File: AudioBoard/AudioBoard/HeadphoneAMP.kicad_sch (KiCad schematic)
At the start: 0 parts

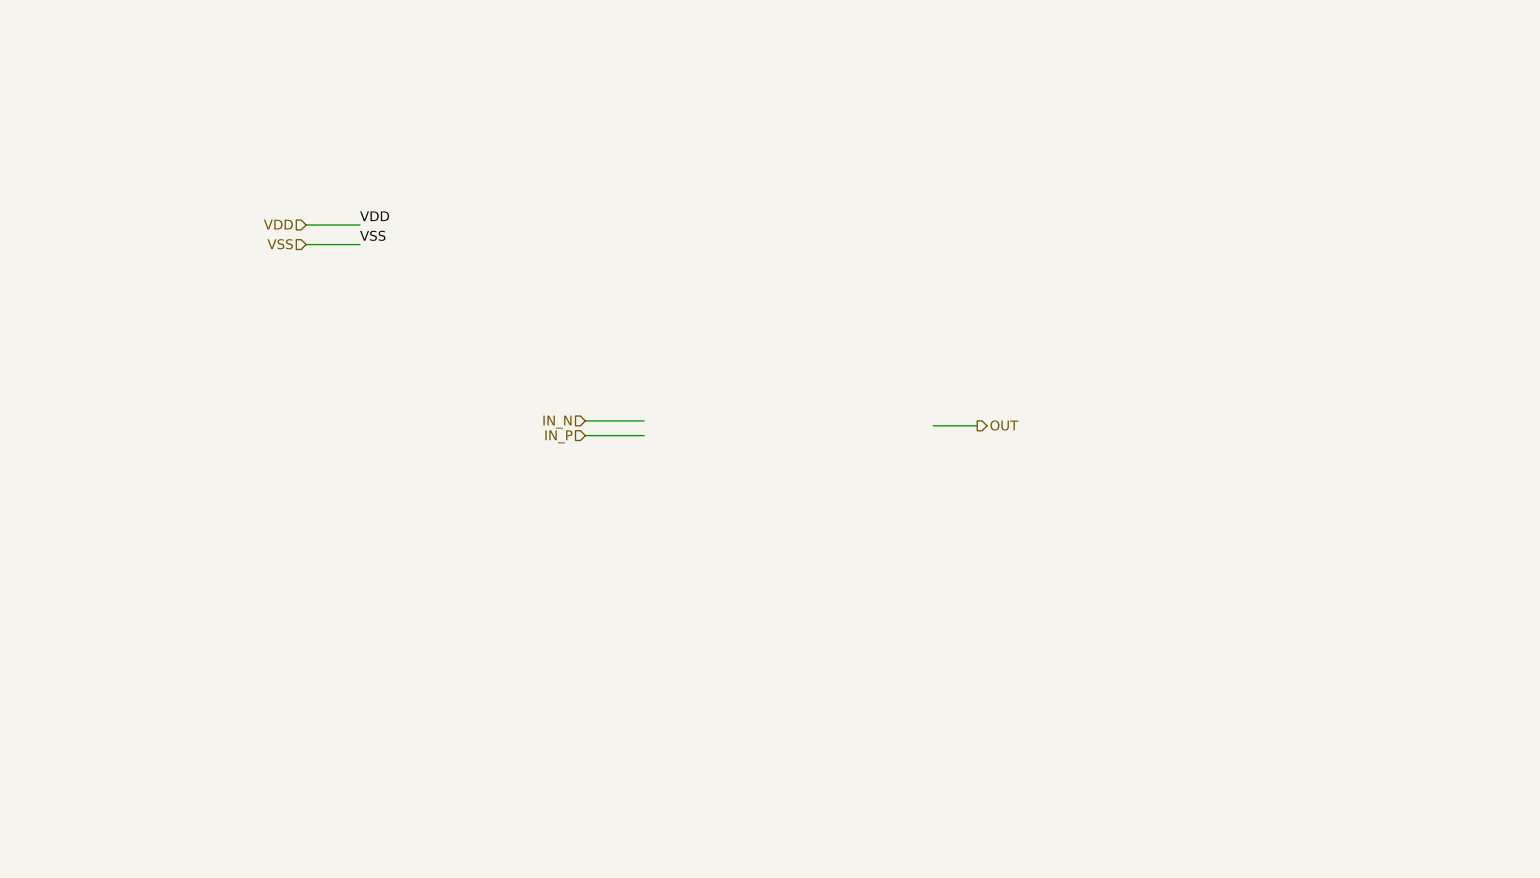
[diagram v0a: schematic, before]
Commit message: added jack IO, headphone amp cirucit
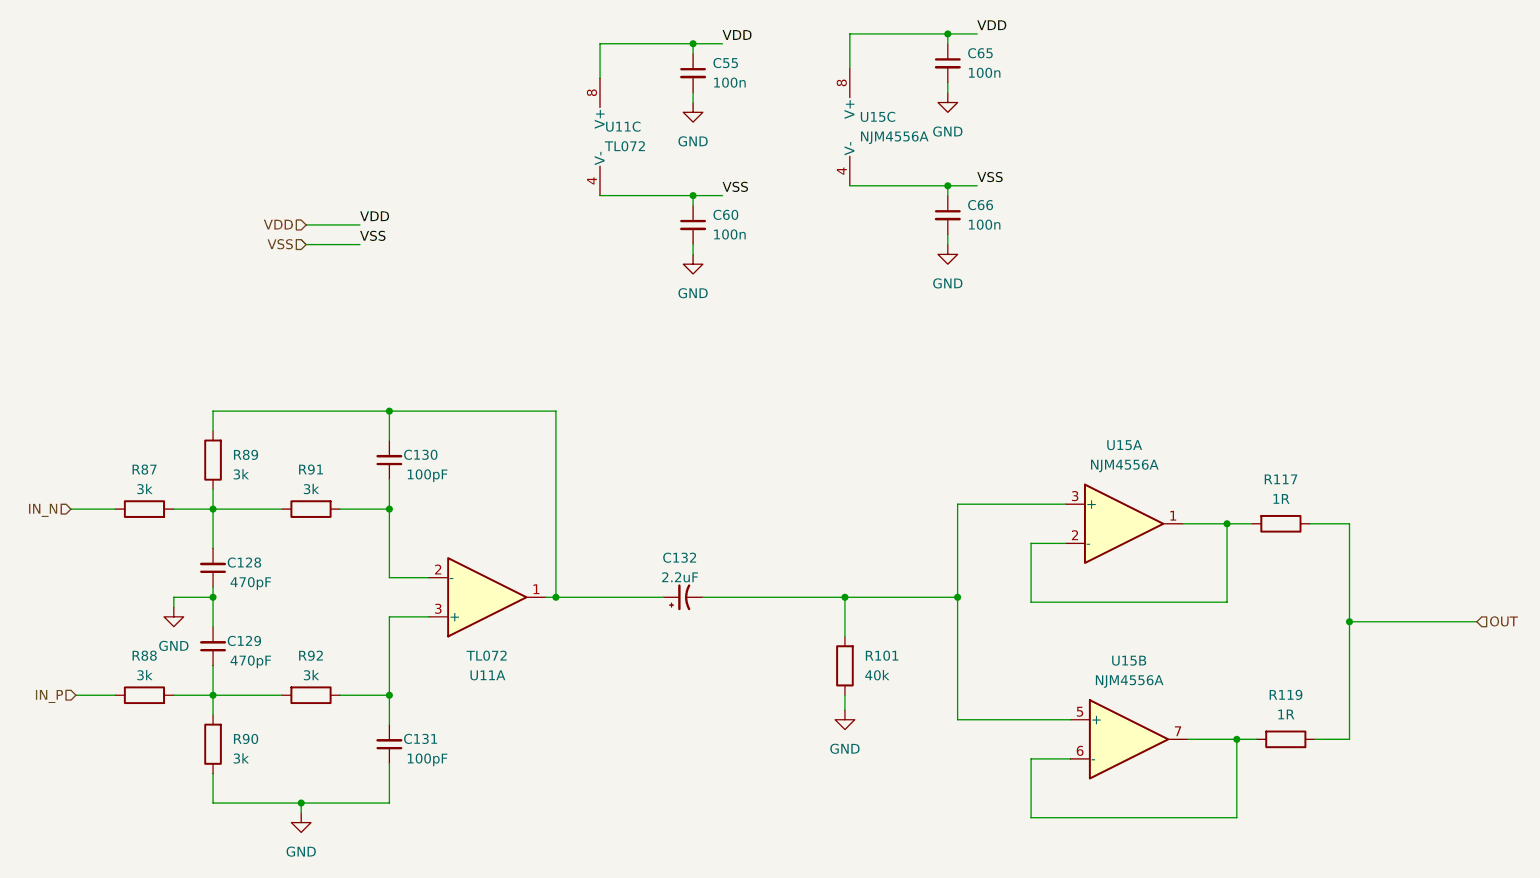
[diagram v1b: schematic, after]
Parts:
- added C128, C129: 470pF, Capacitor_SMD:C_0603_1608Metric, symbol Device:C_Small
- added C130, C131: 100pF, Capacitor_SMD:C_0603_1608Metric, symbol Device:C_Small
- added C132: 2.2uF, Capacitor_SMD:C_0805_2012Metric_Pad1.18x1.45mm_HandSolder, symbol Device:C_Polarized_Small_US
- added C55, C60, C65, C66: 100n, Capacitor_SMD:C_0402_1005Metric, symbol Device:C_Small
- added R101: 40k, Resistor_SMD:R_0603_1608Metric, symbol Device:R
- added R117, R119: 1R, Resistor_SMD:R_0603_1608Metric, symbol Device:R
- added R87, R88, R89, R90, R91, R92: 3k, Resistor_SMD:R_0603_1608Metric, symbol Device:R
- added U11: TL072, symbol Amplifier_Operational:TL072
- added U15: NJM4556A, Package_SO:SOIC-8_5.3x5.3mm_P1.27mm, symbol Amplifier_Operational:NJM4556A
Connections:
- net IN_N: now also R87.1
- net IN_P: now also R88.1
- net OUT: now also R117.1, R119.1
- net VDD: now also C55.1, C65.1, U11.8 (V+), U15.8 (V+)
- net VSS: now also C60.1, C66.1, U11.4 (V-), U15.4 (V-)
- new net: C128.2, R87.2, R89.1, R91.1
- new net: R117.2, U15.1, U15.2 (-)
- new net: C132.2, R101.2, U15.3 (+), U15.5 (+)
- new net: C130.2, C132.1, R89.2, U11.1
- new net: C129.1, R88.2, R90.2, R92.2
- new net: C130.1, R91.2, U11.2 (-)
- new net: C131.2, R92.1, U11.3 (+)
- new net: R119.2, U15.6 (-), U15.7
- new net GND: C128.1, C129.2, C131.1, C55.2, C60.2, C65.2, C66.2, R101.1, R90.1

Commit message: added lcscpart to components and assigned footprints
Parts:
- C55, C60, C65, C66: JLCPCB (none) -> C1591; LCSC Part (none) -> C1591
- U11: footprint (none) -> Package_SO:SOIC-8_3.9x4.9mm_P1.27mm; JLCPCB (none) -> C6961; LCSC Part (none) -> C6961
- U15: JLCPCB (none) -> C3018893; LCSC Part (none) -> C3018893
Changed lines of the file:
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@@
+			)
+		)
+		(property "JLCPCB" "C3018893"
+			(at 167.005 90.805 0)
+			(hide yes)
+			(show_name no)
+			(do_not_autoplace no)
+			(effects
+				(font
+					(size 1.27 1.27)
+				)
+			)
+		)
+		(property "LCSC Part" "C3018893"
+			(at 167.005 90.805 0)
+			(hide yes)
+			(show_name no)
+			(do_not_autoplace no)
+			(effects
+				(font
+					(size 1.27 1.27)
+				)
 			)
 		)
@@
 			)
 		)
+		(property "JLCPCB" "C1591"
+			(at 144.145 50.8 0)
+			(hide yes)
+			(show_name no)
+			(do_not_autoplace no)
+			(effects
+				(font
+					(size 1.27 1.27)
+				)
+			)
+		)
+		(property "LCSC Part" "C1591"
+			(at 144.145 50.8 0)
+			(hide yes)
+			(show_name no)
+			(do_not_autoplace no)
+			(effects
+				(font
+					(size 1.27 1.27)
+				)
+			)
+		)
 		(pin "2"
 		)
@@
 			)
 		)
-		(property "Footprint" ""
+		(property "Footprint" "Package_SO:SOIC-8_3.9x4.9mm_P1.27mm"
 			(at 84.455 100.33 0)
 			(hide yes)
@@
 		)
 		(property "Description" "Dual Low-Noise JFET-Input Operational Amplifiers, DIP-8/SOIC-8"
+			(at 84.455 100.33 0)
+			(hide yes)
+			(show_name no)
+			(do_not_autoplace no)
+			(effects
+				(font
+					(size 1.27 1.27)
+				)
+			)
+		)
+		(property "JLCPCB" "C6961"
+			(at 84.455 100.33 0)
+			(hide yes)
+			(show_name no)
+			(do_not_autoplace no)
+			(effects
+				(font
+					(size 1.27 1.27)
+				)
+			)
+		)
+		(property "LCSC Part" "C6961"
 			(at 84.455 100.33 0)
 			(hide yes)
@@
 			)
 		)
+		(property "JLCPCB" "C1591"
+			(at 144.145 31.115 0)
+			(hide yes)
+			(show_name no)
+			(do_not_autoplace no)
+			(effects
+				(font
+					(size 1.27 1.27)
+				)
+			)
+		)
+		(property "LCSC Part" "C1591"
+			(at 144.145 31.115 0)
+			(hide yes)
+			(show_name no)
+			(do_not_autoplace no)
+			(effects
+				(font
+					(size 1.27 1.27)
+				)
+			)
+		)
 		(pin "2"
 		)
@@
 			)
 		)
+		(property "JLCPCB" "C1591"
+			(at 111.125 32.385 0)
+			(hide yes)
+			(show_name no)
+			(do_not_autoplace no)
+			(effects
+				(font
+					(size 1.27 1.27)
+				)
+			)
+		)
+		(property "LCSC Part" "C1591"
+			(at 111.125 32.385 0)
+			(hide yes)
+			(show_name no)
+			(do_not_autoplace no)
+			(effects
+				(font
+					(size 1.27 1.27)
+				)
+			)
+		)
 		(pin "2"
 		)
@@
 			)
 		)
+		(property "JLCPCB" "C3018893"
+			(at 133.985 39.37 0)
+			(hide yes)
+			(show_name no)
+			(do_not_autoplace no)
+			(effects
+				(font
+					(size 1.27 1.27)
+				)
+			)
+		)
+		(property "LCSC Part" "C3018893"
+			(at 133.985 39.37 0)
+			(hide yes)
+			(show_name no)
+			(do_not_autoplace no)
+			(effects
+				(font
+					(size 1.27 1.27)
+				)
+			)
+		)
 		(pin "5"
 		)
@@
 			)
 		)
+		(property "JLCPCB" "C1591"
+			(at 111.125 52.07 0)
+			(hide yes)
+			(show_name no)
+			(do_not_autoplace no)
+			(effects
+				(font
+					(size 1.27 1.27)
+				)
+			)
+		)
+		(property "LCSC Part" "C1591"
+			(at 111.125 52.07 0)
+			(hide yes)
+			(show_name no)
+			(do_not_autoplace no)
+			(effects
+				(font
+					(size 1.27 1.27)
+				)
+			)
+		)
 		(pin "2"
 		)
@@
 			)
 		)
-		(property "Footprint" ""
+		(property "Footprint" "Package_SO:SOIC-8_3.9x4.9mm_P1.27mm"
 			(at 101.6 40.64 0)
 			(hide yes)
@@
 		)
 		(property "Description" "Dual Low-Noise JFET-Input Operational Amplifiers, DIP-8/SOIC-8"
+			(at 101.6 40.64 0)
+			(hide yes)
+			(show_name no)
+			(do_not_autoplace no)
+			(effects
+				(font
+					(size 1.27 1.27)
+				)
+			)
+		)
+		(property "JLCPCB" "C6961"
+			(at 101.6 40.64 0)
+			(hide yes)
+			(show_name no)
+			(do_not_autoplace no)
+			(effects
+				(font
+					(size 1.27 1.27)
+				)
+			)
+		)
+		(property "LCSC Part" "C6961"
 			(at 101.6 40.64 0)
 			(hide yes)
@@
 			(at 167.64 118.745 0)
 			(hide yes)
+			(show_name no)
+			(do_not_autoplace no)
+			(effects
+				(font
+					(size 1.27 1.27)
+				)
+			)
+		)
+		(property "JLCPCB" "C3018893"
+			(at 167.64 118.745 0)
+			(hide yes)
+			(show_name no)
+			(do_not_autoplace no)
+			(effects
+				(font
+					(size 1.27 1.27)
+				)
+			)
+		)
+		(property "LCSC Part" "C3018893"
+			(at 167.64 118.745 0)
+			(hide yes)
